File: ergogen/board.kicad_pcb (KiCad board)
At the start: 2 copper layers, 154.2 x 107.9 mm, 58 parts

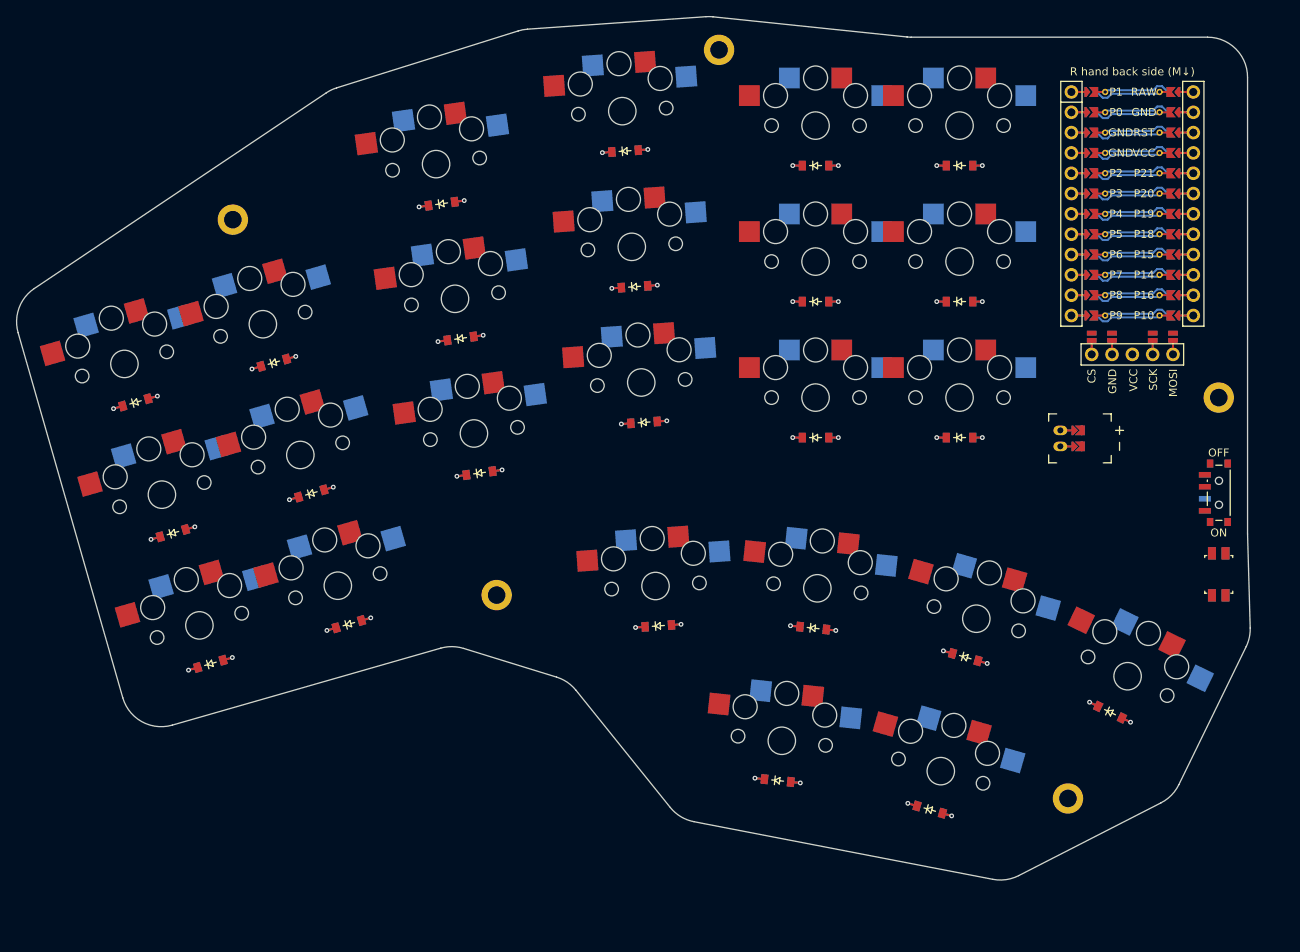
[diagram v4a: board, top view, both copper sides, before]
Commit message: using better footprint for key switches
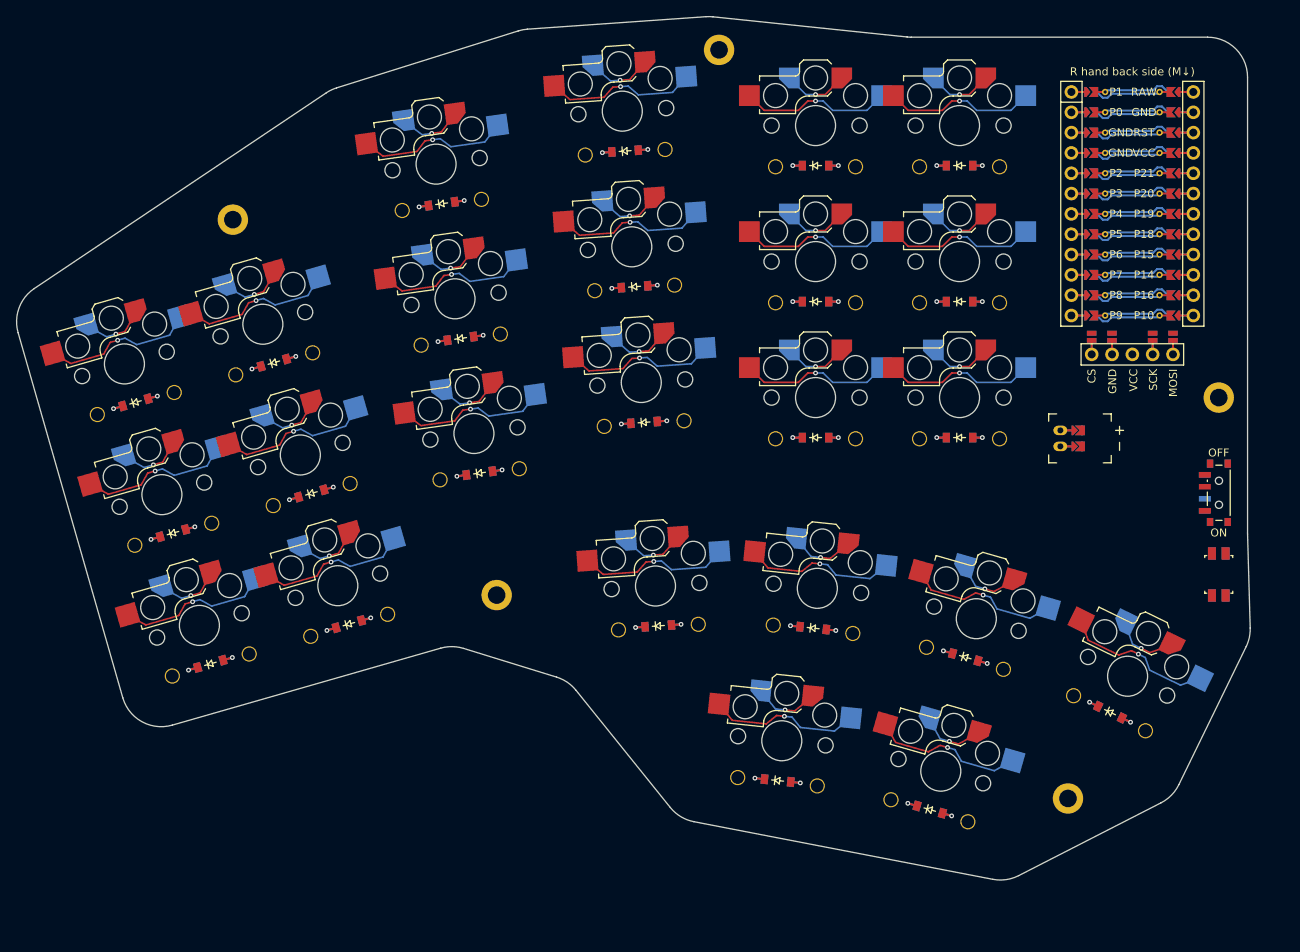
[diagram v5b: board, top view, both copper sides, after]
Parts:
- S1, S10, S11, S12, S13, S14, S15, S16, S17, S18, S19, S2, S20, S21, S22, S23, S24, S3, S4, S5, S6, S7, S8, S9: footprint PG1350 -> ceoloide:switch_choc_v1_v2; moved to B.Cu
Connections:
- D1 pad 1: P18 -> P19
- D10 pad 1: P18 -> P19
- D11 pad 1: P19 -> P20
- D12 pad 1: P20 -> P21
- D13 pad 1: P18 -> P19
- D14 pad 1: P19 -> P20
- D15 pad 1: P20 -> P21
- D16 pad 1: P18 -> P19
- D17 pad 1: P19 -> P20
- D18 pad 1: P20 -> P21
- D19 pad 1: P21 -> P18
- D2 pad 1: P19 -> P20
- D20 pad 1: P21 -> P18
- D21 pad 1: P21 -> P18
- D22 pad 1: P21 -> P18
- D23 pad 1: P21 -> P18
- D24 pad 1: P21 -> P18
- D3 pad 1: P20 -> P21
- D4 pad 1: P18 -> P19
- D5 pad 1: P19 -> P20
- D6 pad 1: P20 -> P21
- D7 pad 1: P18 -> P19
- D8 pad 1: P19 -> P20
- D9 pad 1: P20 -> P21
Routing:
- net P10: track 0.00 -> 33.1 mm, vias 0 -> 4
- net P8: track 0.00 -> 33.1 mm, vias 0 -> 4
- net P9: track 0.00 -> 33.1 mm, vias 0 -> 4
- net P15: track 0.00 -> 33.1 mm, vias 0 -> 4
- net P16: track 0.00 -> 33.1 mm, vias 0 -> 4
- net P14: track 0.00 -> 33.1 mm, vias 0 -> 4
- net ring_top: track 2.40 -> 21.5 mm, vias 1 -> 2
- net ring_home: track 2.40 -> 21.5 mm, vias 1 -> 2
- net ring_bottom: track 2.40 -> 21.5 mm, vias 1 -> 2
- net inner_top: track 2.40 -> 21.5 mm, vias 1 -> 2
- net inner_home: track 2.40 -> 21.5 mm, vias 1 -> 2
- net inner_bottom: track 2.40 -> 21.5 mm, vias 1 -> 2
- net index_top: track 2.40 -> 21.5 mm, vias 1 -> 2
- net index_home: track 2.40 -> 21.5 mm, vias 1 -> 2
- net index_bottom: track 2.40 -> 21.5 mm, vias 1 -> 2
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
